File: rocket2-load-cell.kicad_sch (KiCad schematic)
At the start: 41 parts, among them J1 SWD, J2 Screw_Terminal_01x02, J3 629105150521, U1 STM32F103C8Tx, U2 AMS1117-3.3, Y1 16MHz

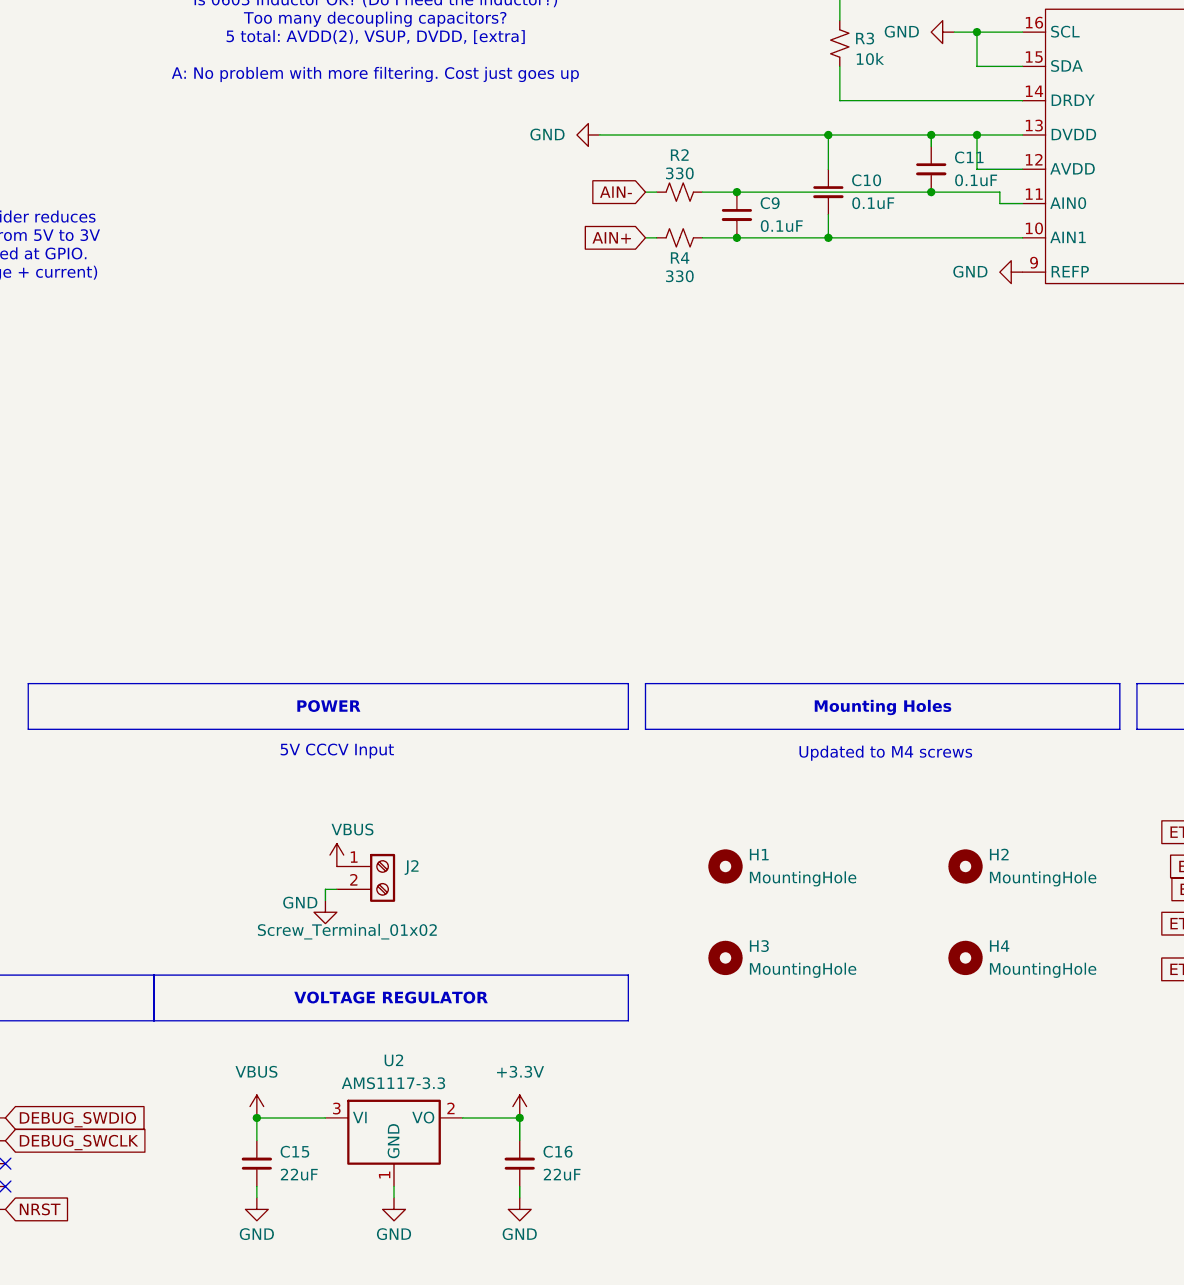
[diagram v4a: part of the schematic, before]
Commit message: Barrel Jack, New Regulator, and Full Routing
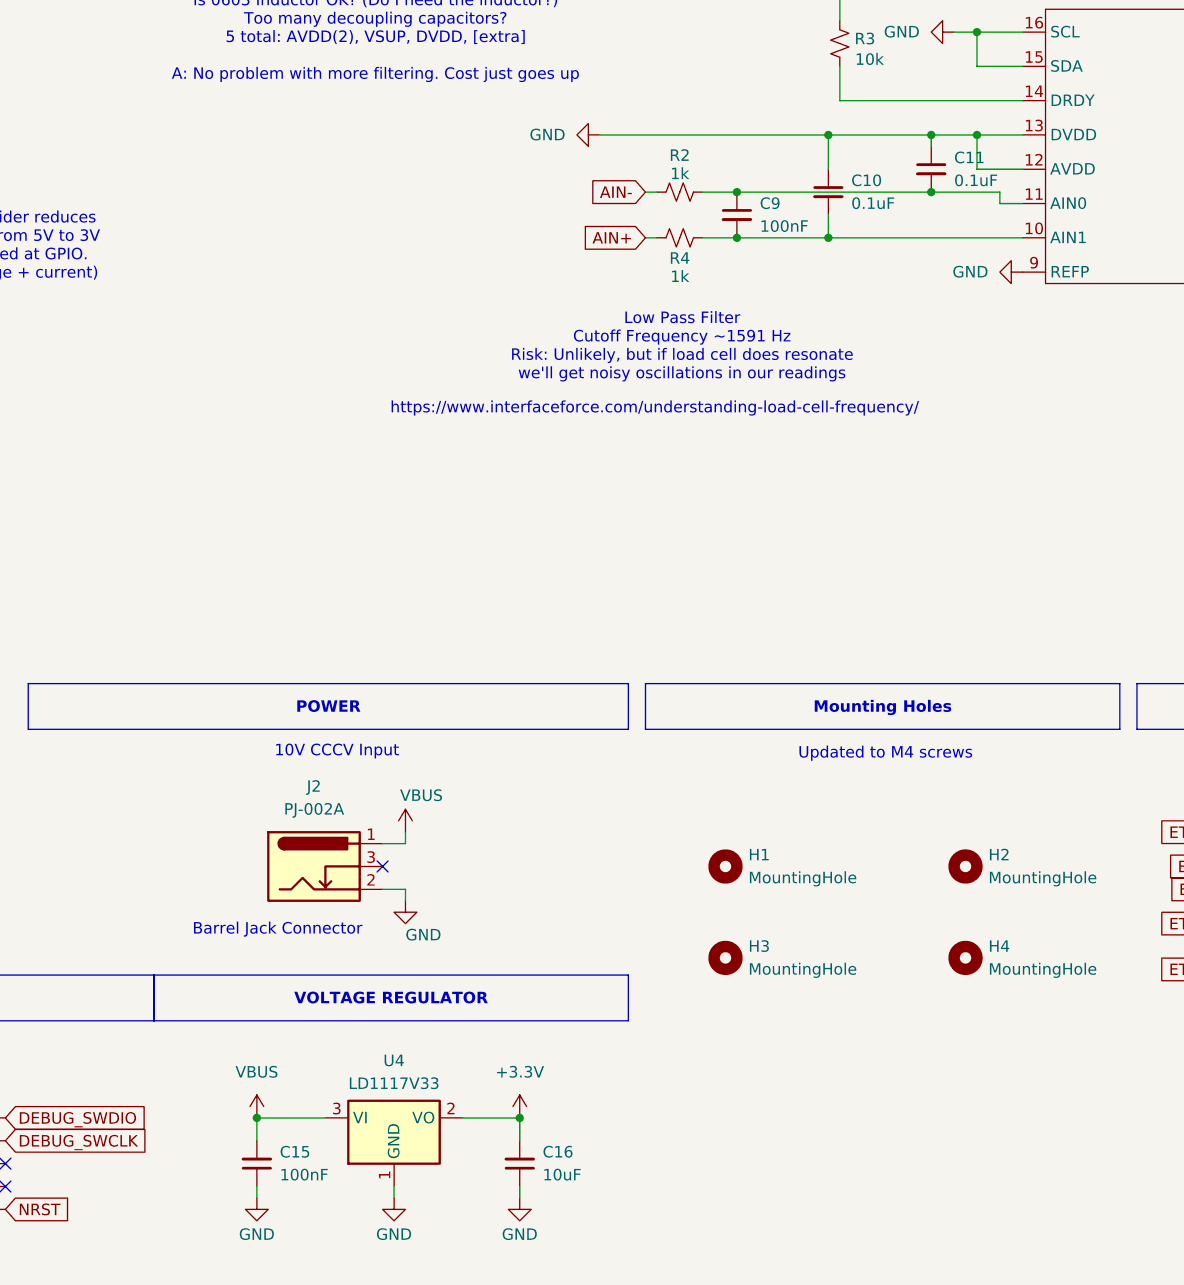
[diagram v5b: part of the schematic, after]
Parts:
- removed J2: Screw_Terminal_01x02, TerminalBlock_Phoenix:TerminalBlock_Phoenix_MKDS-1,5-2-5.08_1x02_P5.08mm_Horizontal, symbol Connector:Screw_Terminal_01x02
- removed U2: AMS1117-3.3, Package_TO_SOT_SMD:SOT-223-3_TabPin2, symbol Regulator_Linear:AMS1117-3.3
- added J2: PJ-002A, UCIRP-KiCAD-Lib:CUI_PJ-202A, symbol Connector:Barrel_Jack_Switch
- added U4: LD1117V33, Package_TO_SOT_THT:TO-220-3_Vertical, symbol Regulator_Linear:LD1117V33
- C15: value 22uF -> 100nF
- C16: value 22uF -> 10uF
- C9: value 0.1uF -> 100nF
- R2, R4: value 330 -> 1k
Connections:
- net +3.3V: now also U4.2 (VO)
- net GND: now also J2.2, U4.1 (GND)
- net VBUS: now also J2.1, U4.3 (VI)
- no-connect marks 31 -> 32
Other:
- note added: "10V CCCV Input"
- note added: "Barrel Jack Connector"
- note added: "Low Pass Filter Cutoff Frequency ~1591 Hz Risk: Unlikely, but if load cell does resonate we'll get noisy oscillations in our readings"
- note added: "https://www.interfaceforce.com/understanding-load-cell-frequency/"
- note removed: "5V CCCV Input"

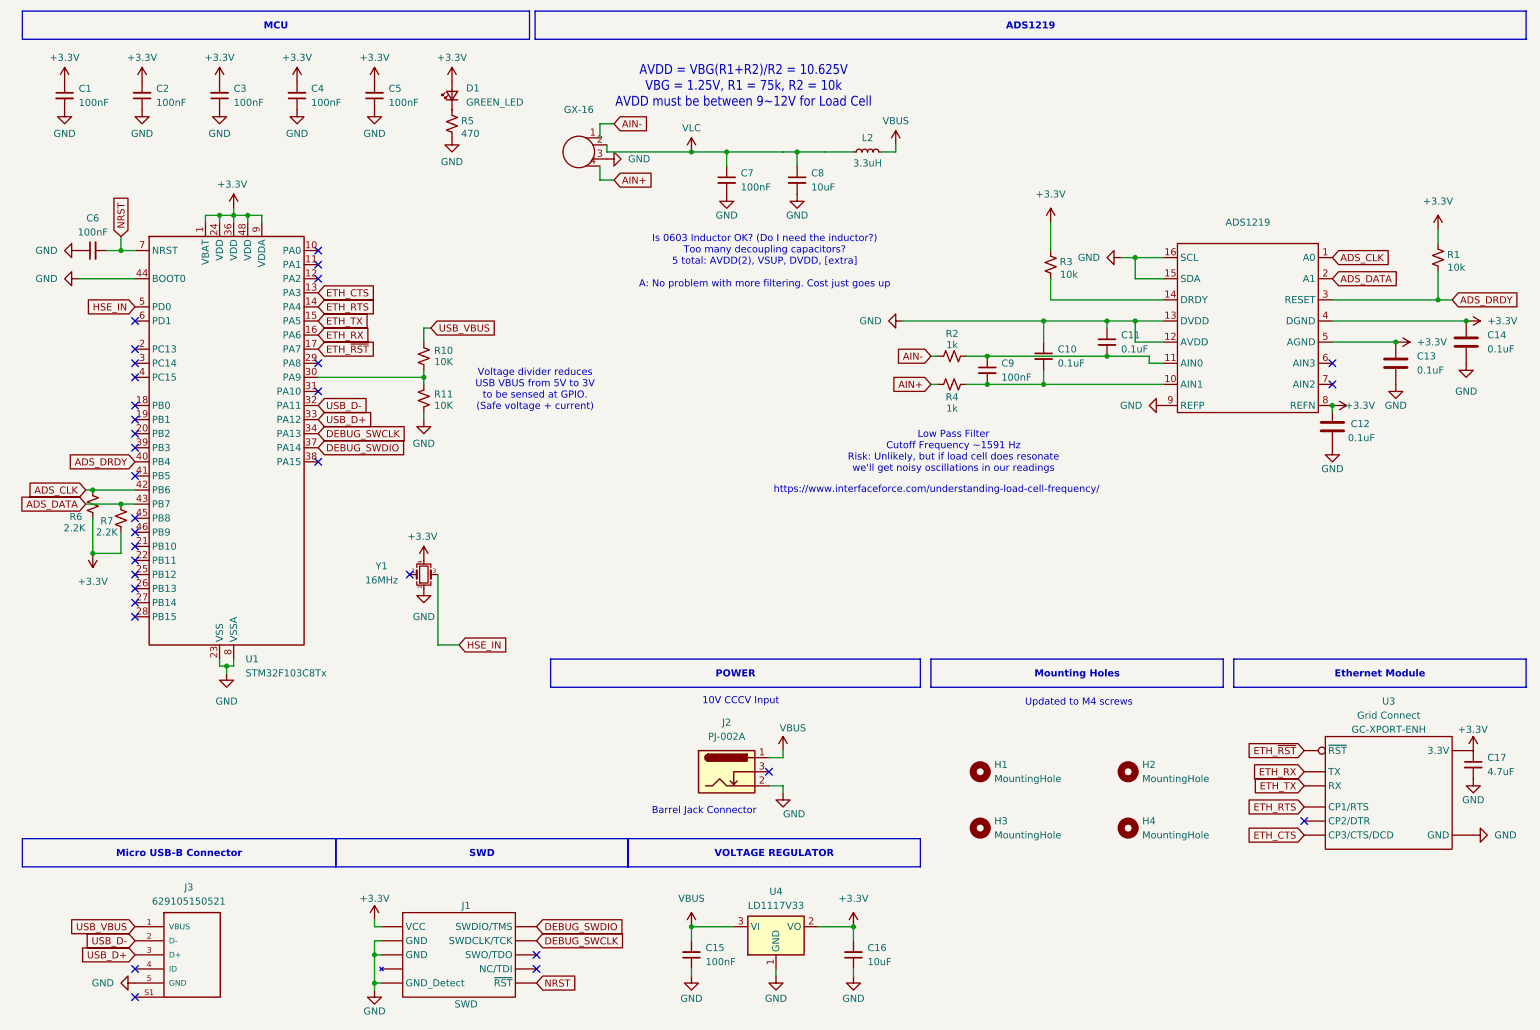
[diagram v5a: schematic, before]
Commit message: Updated based on DRC
Filled zones filled
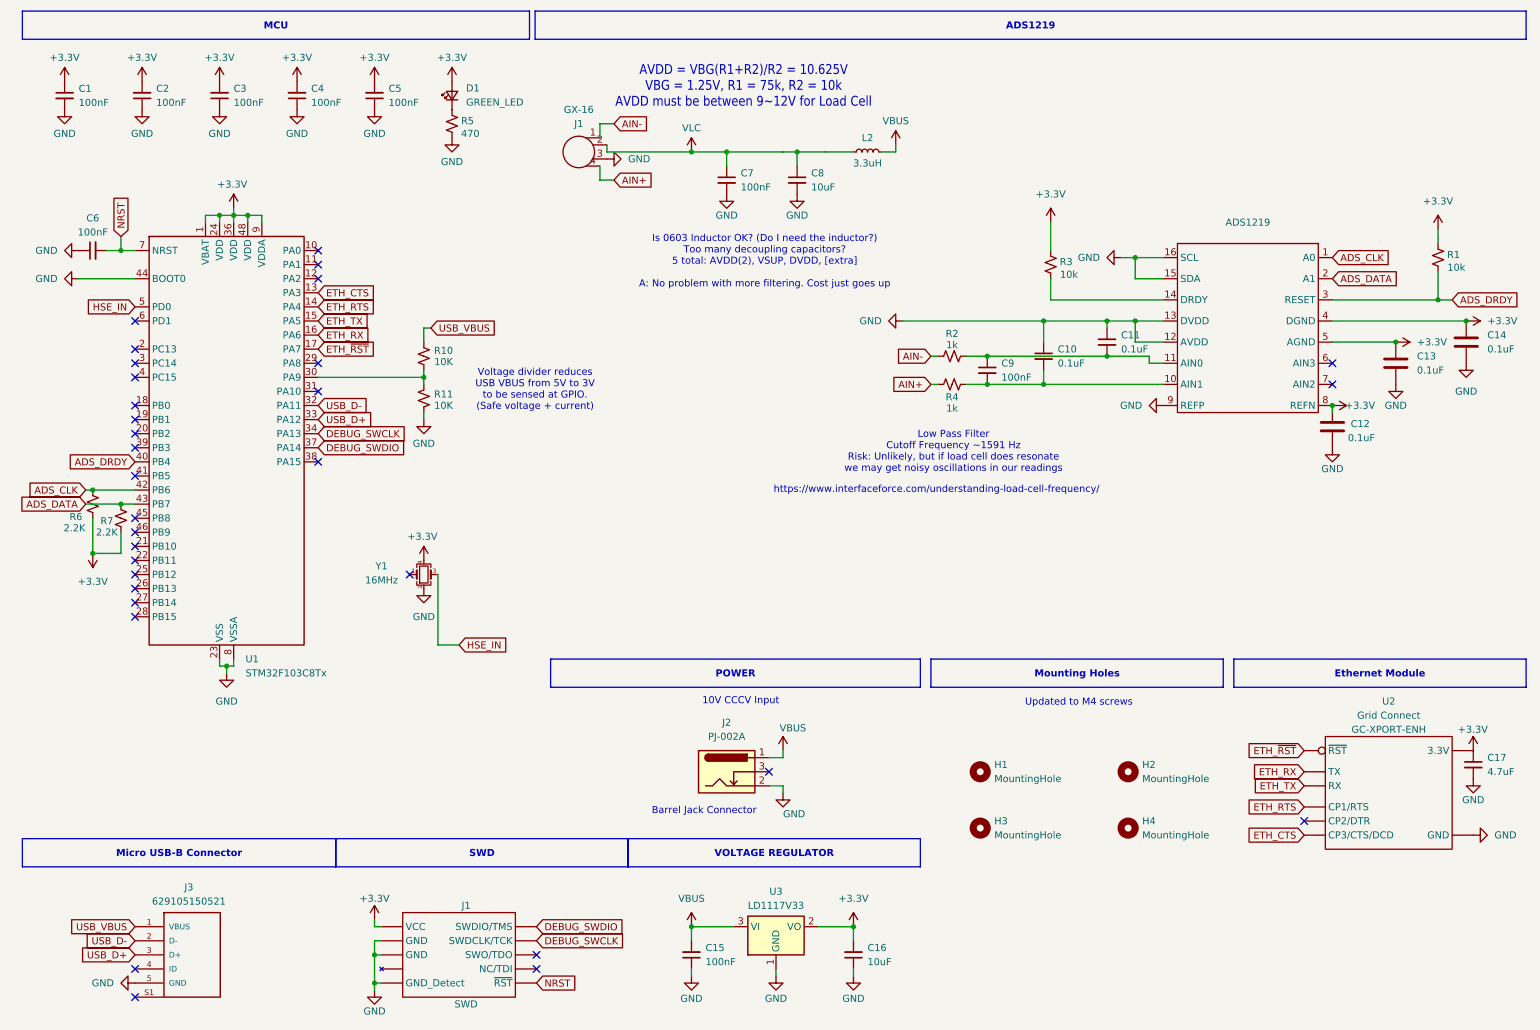
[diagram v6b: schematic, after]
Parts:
- GX-16: value ~ -> J1
- renumbered U3 to U2, U4 to U3
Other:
- note added: "Low Pass Filter Cutoff Frequency ~1591 Hz Risk: Unlikely, but if load cell does resonate we may get noisy oscillations in our readings"
- note removed: "Low Pass Filter Cutoff Frequency ~1591 Hz Risk: Unlikely, but if load cell does resonate we'll get noisy oscillations in our readings"
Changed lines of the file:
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@@
 		)
 	)
-	(text "Low Pass Filter\nCutoff Frequency ~1591 Hz\nRisk: Unlikely, but if load cell does resonate\nwe'll get noisy oscillations in our readings"
+	(text "Low Pass Filter\nCutoff Frequency ~1591 Hz\nRisk: Unlikely, but if load cell does resonate\nwe may get noisy oscillations in our readings"
 		(exclude_from_sim no)
 		(at 180.594 92.202 0)
@@
 			)
 		)
-		(property "Value" "~"
+		(property "Value" "J1"
 			(at 113.03 33.02 0)
 			(effects
@@
 		(dnp no)
 		(fields_autoplaced yes)
-		(property "Reference" "U4"
+		(property "Reference" "U3"
 			(at 148.59 171.45 0)
 			(effects
@@
 			(project ""
 				(path "/d1f04dc8-a56c-4379-8ad0-2916e7244fc3"
-					(reference "U4")
+					(reference "U3")
 					(unit 1)
 				)
@@
 		(on_board yes)
 		(dnp no)
-		(property "Reference" "U3"
+		(property "Reference" "U2"
 			(at 259.08 137.16 0)
 			(effects
@@
 			(project "rocket2-load-cell"
 				(path "/d1f04dc8-a56c-4379-8ad0-2916e7244fc3"
-					(reference "U3")
+					(reference "U2")
 					(unit 1)
 				)

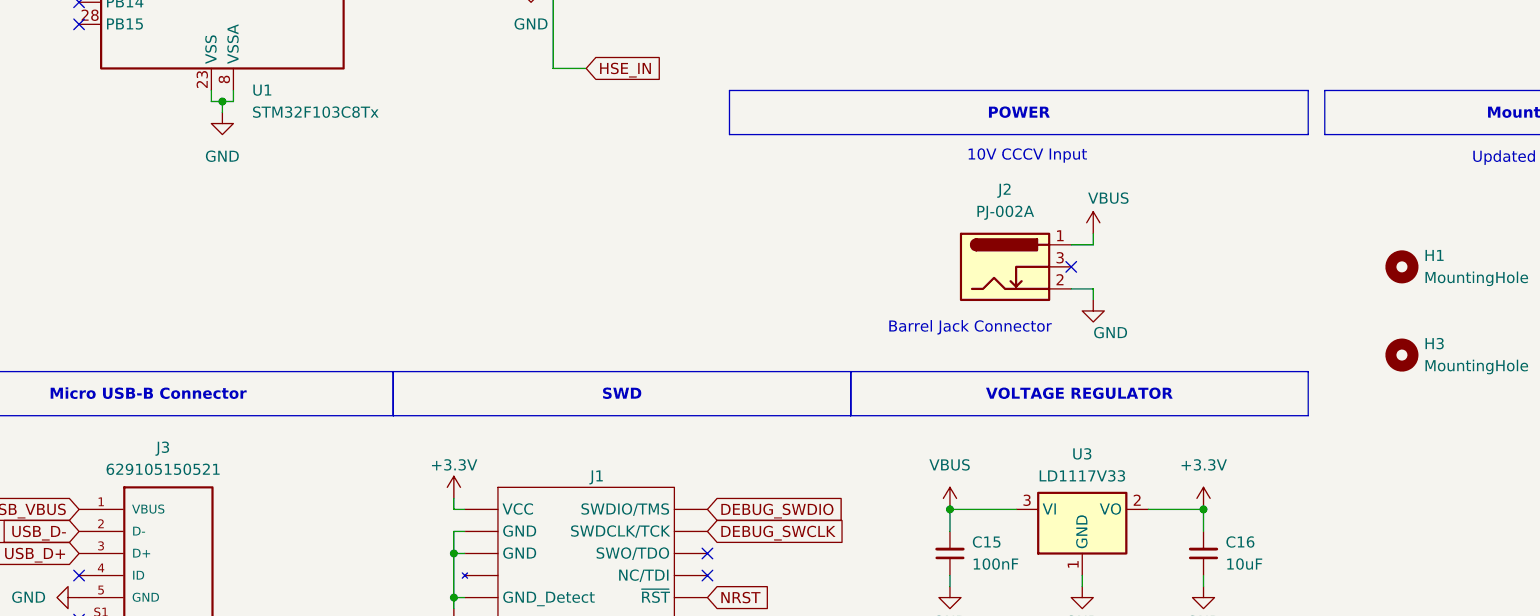
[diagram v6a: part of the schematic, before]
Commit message: Added Through-hole Backup Power
Redundancy for the barrel jack
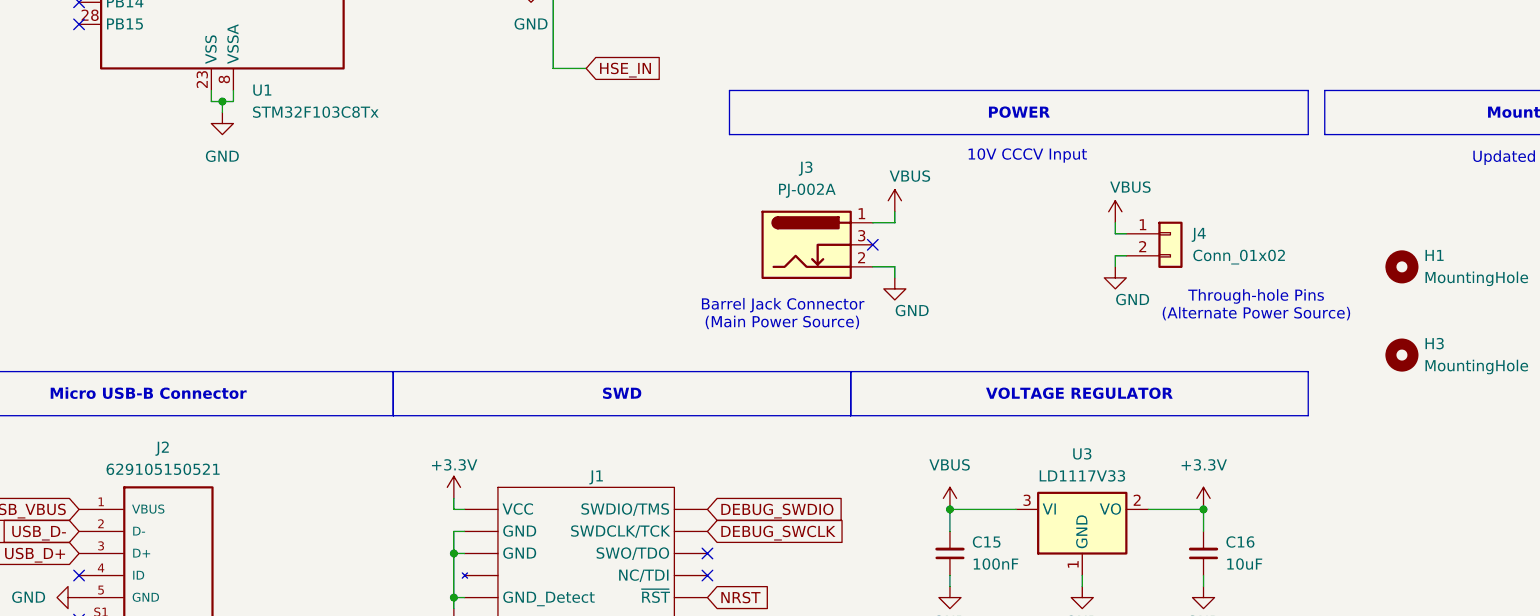
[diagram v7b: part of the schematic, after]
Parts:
- added J4: Conn_01x02, Connector_Wire:SolderWire-0.1sqmm_1x02_P3.6mm_D0.4mm_OD1mm, symbol Connector_Generic:Conn_01x02
- renumbered J3 to J2, J2 to J3
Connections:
- net GND: now also J4.2 (Pin_2)
- net VBUS: now also J4.1 (Pin_1)
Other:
- note added: "Barrel Jack Connector (Main Power Source)"
- note added: "Through-hole Pins (Alternate Power Source)"
- note removed: "Barrel Jack Connector"
- moved on the sheet: J3

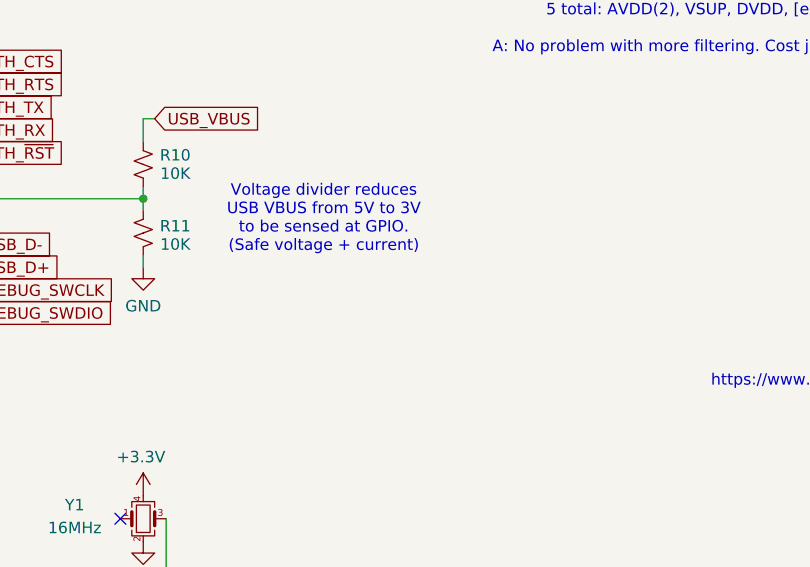
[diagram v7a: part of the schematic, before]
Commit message: Final Updates
Adjusted GX16, reduced E-footprint
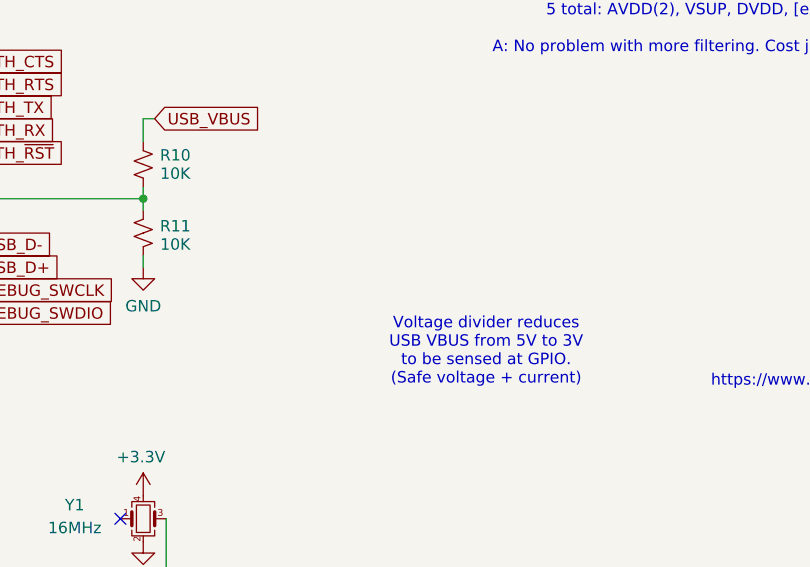
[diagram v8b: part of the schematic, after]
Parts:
- J4: footprint Connector_Wire:SolderWire-0.1sqmm_1x02_P3.6mm_D0.4mm_OD1mm -> (none)
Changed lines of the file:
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@@
 	(text "Voltage divider reduces \nUSB VBUS from 5V to 3V \nto be sensed at GPIO.\n(Safe voltage + current)\n"
 		(exclude_from_sim no)
-		(at 105.156 81.026 0)
+		(at 123.19 95.758 0)
 		(effects
 			(font
@@
 		(on_board yes)
 		(dnp no)
-		(fields_autoplaced yes)
 		(property "Reference" "J3"
 			(at 116.84 138.43 0)
@@
 			)
 		)
-		(property "Footprint" "Connector_Wire:SolderWire-0.1sqmm_1x02_P3.6mm_D0.4mm_OD1mm"
+		(property "Footprint" ""
 			(at 158.75 146.05 0)
 			(effects
